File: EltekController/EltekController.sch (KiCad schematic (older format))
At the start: 36 parts, among them J1 CANBUS, J2 ESP-PROG, J3 Qwiic, SW1 RST, SW2 BOOT, SW3 LEFT, SW4 SEL, SW5 RIGHT, U1 ESP32-S2-WROVER, U2 MAX3051ESA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

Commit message: switch to nano-fit, but any 2.54 or 2.5mm header works
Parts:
- J1: footprint SnapEDA-zip:TE_5-103634-3 -> 11-My-Edits:Molex_Nano-Fit_105313-xx04_1x04_P2.50mm_Horizontal_3D
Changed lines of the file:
@@
 F 0 "J1" H 10668 5767 50  0000 C CNN
 F 1 "CANBUS" H 10668 5676 50  0000 C CNN
-F 2 "SnapEDA-zip:TE_5-103634-3" H 10750 5450 50  0001 C CNN
+F 2 "11-My-Edits:Molex_Nano-Fit_105313-xx04_1x04_P2.50mm_Horizontal_3D" H 10750 5450 50  0001 C CNN
 F 3 "~" H 10750 5450 50  0001 C CNN
 	1    10750 5450

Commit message: missed a trace
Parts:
- U2: JLCPCB_CORRECTION 0;0;270 -> 0;0;-90
- U3: JLCPCB_CORRECTION 0;0;180 -> 0;0;-180
- USB1: JLCPCB_CORRECTION 0;0;270 -> 0;0;0
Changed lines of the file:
@@
 F 5 "Maxim" H 2750 5250 50  0001 C CNN "Manufacturer"
 F 6 "MAX3051ESA+T" H 2750 5250 50  0001 C CNN "MPN"
-F 7 "0;0;270" H 2750 5250 50  0001 C CNN "JLCPCB_CORRECTION"
+F 7 "0;0;-90" H 2750 5250 50  0001 C CNN "JLCPCB_CORRECTION"
 	1    2750 5250
 	1    0    0    -1
@@
 F 3 "~" H 1850 1900 50  0001 C CNN
 F 4 "C397452" H 1700 1950 50  0001 C CNN "LCSC"
-F 5 "0;0;270" H 1700 1950 50  0001 C CNN "JLCPCB_CORRECTION"
+F 5 "0;0;0" H 1700 1950 50  0001 C CNN "JLCPCB_CORRECTION"
 	1    1700 1950
 	1    0    0    -1
@@
 F 3 "https://www.torexsemi.com/file/xc6220/XC6220.pdf" H 4000 850 50  0001 C CNN
 F 4 "C86534" H 3250 1850 50  0001 C CNN "LCSC"
-F 5 "0;0;180" H 3250 1850 50  0001 C CNN "JLCPCB_CORRECTION"
+F 5 "0;0;-180" H 3250 1850 50  0001 C CNN "JLCPCB_CORRECTION"
 	1    3250 1850
 	1    0    0    -1

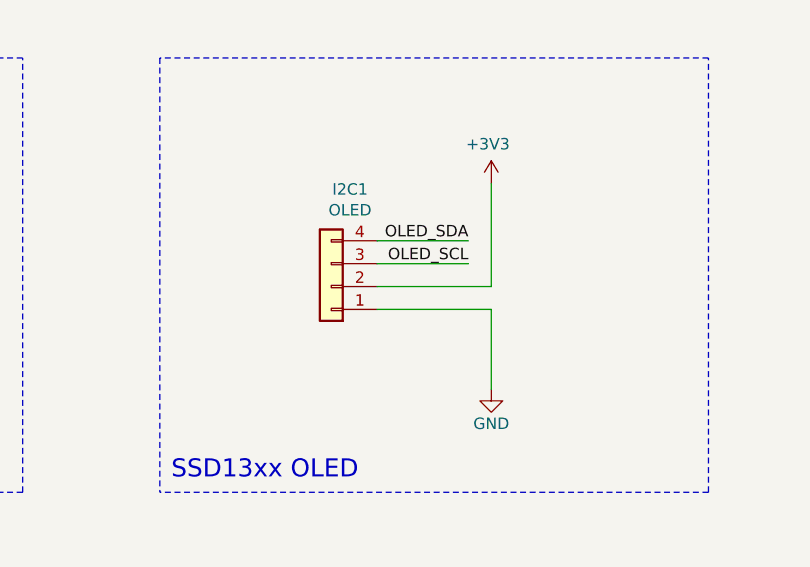
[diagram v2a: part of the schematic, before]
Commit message: flip VCC and GND on the OLED... sigh
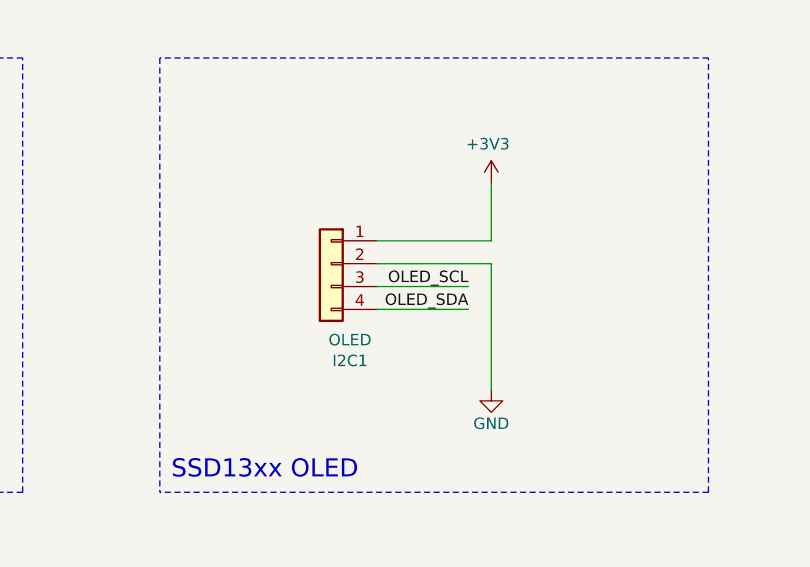
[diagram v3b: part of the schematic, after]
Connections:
- net +3V3: now also I2C1.1 (Pin_1); no longer I2C1.2 (Pin_2)
- net GND: now also I2C1.2 (Pin_2); no longer I2C1.1 (Pin_1)
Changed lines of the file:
@@
 $EndComp
 Wire Wire Line
-	14000 5450 14400 5450
+	14000 5550 14400 5550
 Wire Wire Line
-	14000 5350 14400 5350
+	14000 5650 14400 5650
 $Comp
 L Connector_Generic:Conn_01x04 I2C1
 U 1 1 6036EBBD
-P 13800 5550
-F 0 "I2C1" H 13718 5125 50  0000 C CNN
-F 1 "OLED" H 13718 5216 50  0000 C CNN
-F 2 "10-My-Footprints:OLED_SSD1315_128x64_1.3_I2C_New_Silhouette_Big3D" H 13880 5405 50  0001 L CNN
-F 3 "~" H 13800 5550 50  0001 C CNN
-	1    13800 5550
-	-1   0    0    1
+P 13800 5450
+F 0 "I2C1" H 13718 5025 50  0000 C CNN
+F 1 "OLED" H 13718 5116 50  0000 C CNN
+F 2 "10-My-Footprints:OLED_SSD1315_128x64_1.3_I2C_New_Silhouette_Big3D" H 13880 5305 50  0001 L CNN
+F 3 "~" H 13800 5450 50  0001 C CNN
+	1    13800 5450
+	-1   0    0    -1
 $EndComp
 $Comp
@@
 	-1   0    0    -1
 $EndComp
-Text Label 14400 5450 2    50   ~ 0
+Text Label 14400 5550 2    50   ~ 0
 OLED_SCL
-Text Label 14400 5350 2    50   ~ 0
+Text Label 14400 5650 2    50   ~ 0
 OLED_SDA
 Text Notes 13100 6400 0    79   ~ 0
@@
 	3500 4750 3750 4750
 Wire Wire Line
-	14500 5100 14500 5550
+	14500 5100 14500 5350
 Wire Wire Line
-	14000 5550 14500 5550
+	14000 5450 14500 5450
 Wire Wire Line
-	14000 5650 14500 5650
+	14000 5350 14500 5350
 Wire Wire Line
-	14500 5650 14500 6000
+	14500 5450 14500 6000
 Wire Notes Line
 	12450 1050 10050 1050

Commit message: Revert "flip VCC and GND on the OLED... sigh"
This reverts commit 16d08c3f3e759163bdd9650e3550ba9f731368f2.
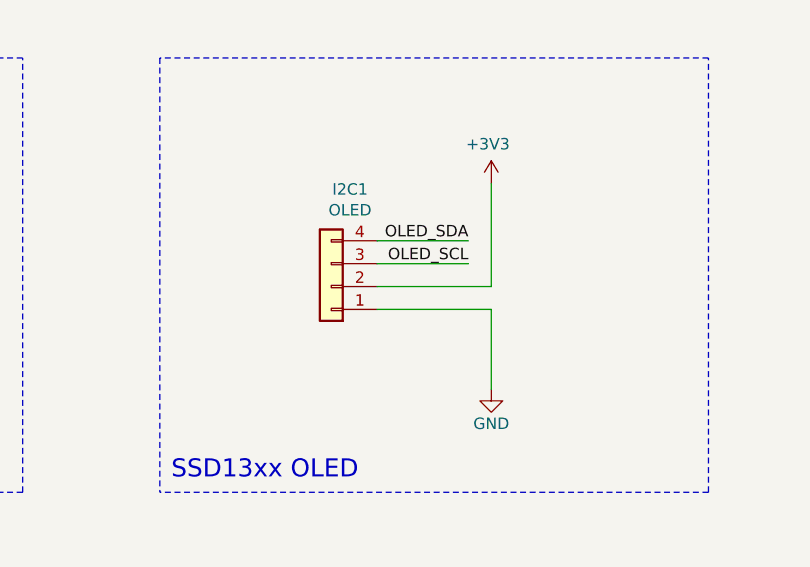
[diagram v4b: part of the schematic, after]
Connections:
- net +3V3: now also I2C1.2 (Pin_2); no longer I2C1.1 (Pin_1)
- net GND: now also I2C1.1 (Pin_1); no longer I2C1.2 (Pin_2)
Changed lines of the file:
@@
 $EndComp
 Wire Wire Line
-	14000 5550 14400 5550
+	14000 5450 14400 5450
 Wire Wire Line
-	14000 5650 14400 5650
+	14000 5350 14400 5350
 $Comp
 L Connector_Generic:Conn_01x04 I2C1
 U 1 1 6036EBBD
-P 13800 5450
-F 0 "I2C1" H 13718 5025 50  0000 C CNN
-F 1 "OLED" H 13718 5116 50  0000 C CNN
-F 2 "10-My-Footprints:OLED_SSD1315_128x64_1.3_I2C_New_Silhouette_Big3D" H 13880 5305 50  0001 L CNN
-F 3 "~" H 13800 5450 50  0001 C CNN
-	1    13800 5450
-	-1   0    0    -1
+P 13800 5550
+F 0 "I2C1" H 13718 5125 50  0000 C CNN
+F 1 "OLED" H 13718 5216 50  0000 C CNN
+F 2 "10-My-Footprints:OLED_SSD1315_128x64_1.3_I2C_New_Silhouette_Big3D" H 13880 5405 50  0001 L CNN
+F 3 "~" H 13800 5550 50  0001 C CNN
+	1    13800 5550
+	-1   0    0    1
 $EndComp
 $Comp
@@
 	-1   0    0    -1
 $EndComp
-Text Label 14400 5550 2    50   ~ 0
+Text Label 14400 5450 2    50   ~ 0
 OLED_SCL
-Text Label 14400 5650 2    50   ~ 0
+Text Label 14400 5350 2    50   ~ 0
 OLED_SDA
 Text Notes 13100 6400 0    79   ~ 0
@@
 	3500 4750 3750 4750
 Wire Wire Line
-	14500 5100 14500 5350
+	14500 5100 14500 5550
 Wire Wire Line
-	14000 5450 14500 5450
+	14000 5550 14500 5550
 Wire Wire Line
-	14000 5350 14500 5350
+	14000 5650 14500 5650
 Wire Wire Line
-	14500 5450 14500 6000
+	14500 5650 14500 6000
 Wire Notes Line
 	12450 1050 10050 1050
